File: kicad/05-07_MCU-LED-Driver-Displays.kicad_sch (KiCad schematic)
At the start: 68 parts, among them J4 Conn_02x05_Counter_Clockwise, J5 Conn_01x02_Pin, J6 Conn_01x03_Pin, J7 Conn_01x03_Pin, Q4 AO3400A, Q5 AO3400A, SW1 BOOTSEL, SW2 RESET, SW3 USER_A, SW4 USER_B_PWR, U5 W25Q128JVS, U6 PCF8523T, U7 RP2040, Y1 ABS07AIG-32.768KHZ-7-T, Y2 ABM8-272-T3

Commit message: DR SYS-04-Battery Protect ✅
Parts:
- R19, R20, R21, R22, R23, R24, R25, R26, R27, R28, R29, R30, R31, R32, R33, R34, R35, R36, R37, R38, R39: MPN (none) -> (Generic)
- renumbered JP12 to JP14, JP13 to JP15, JP14 to JP16, JP15 to JP17, JP16 to JP18, JP17 to JP19, JP18 to JP20, JP19 to JP21, TP17 to TP18, TP18 to TP19, TP19 to TP20, TP20 to TP21, TP21 to TP22, TP22 to TP23

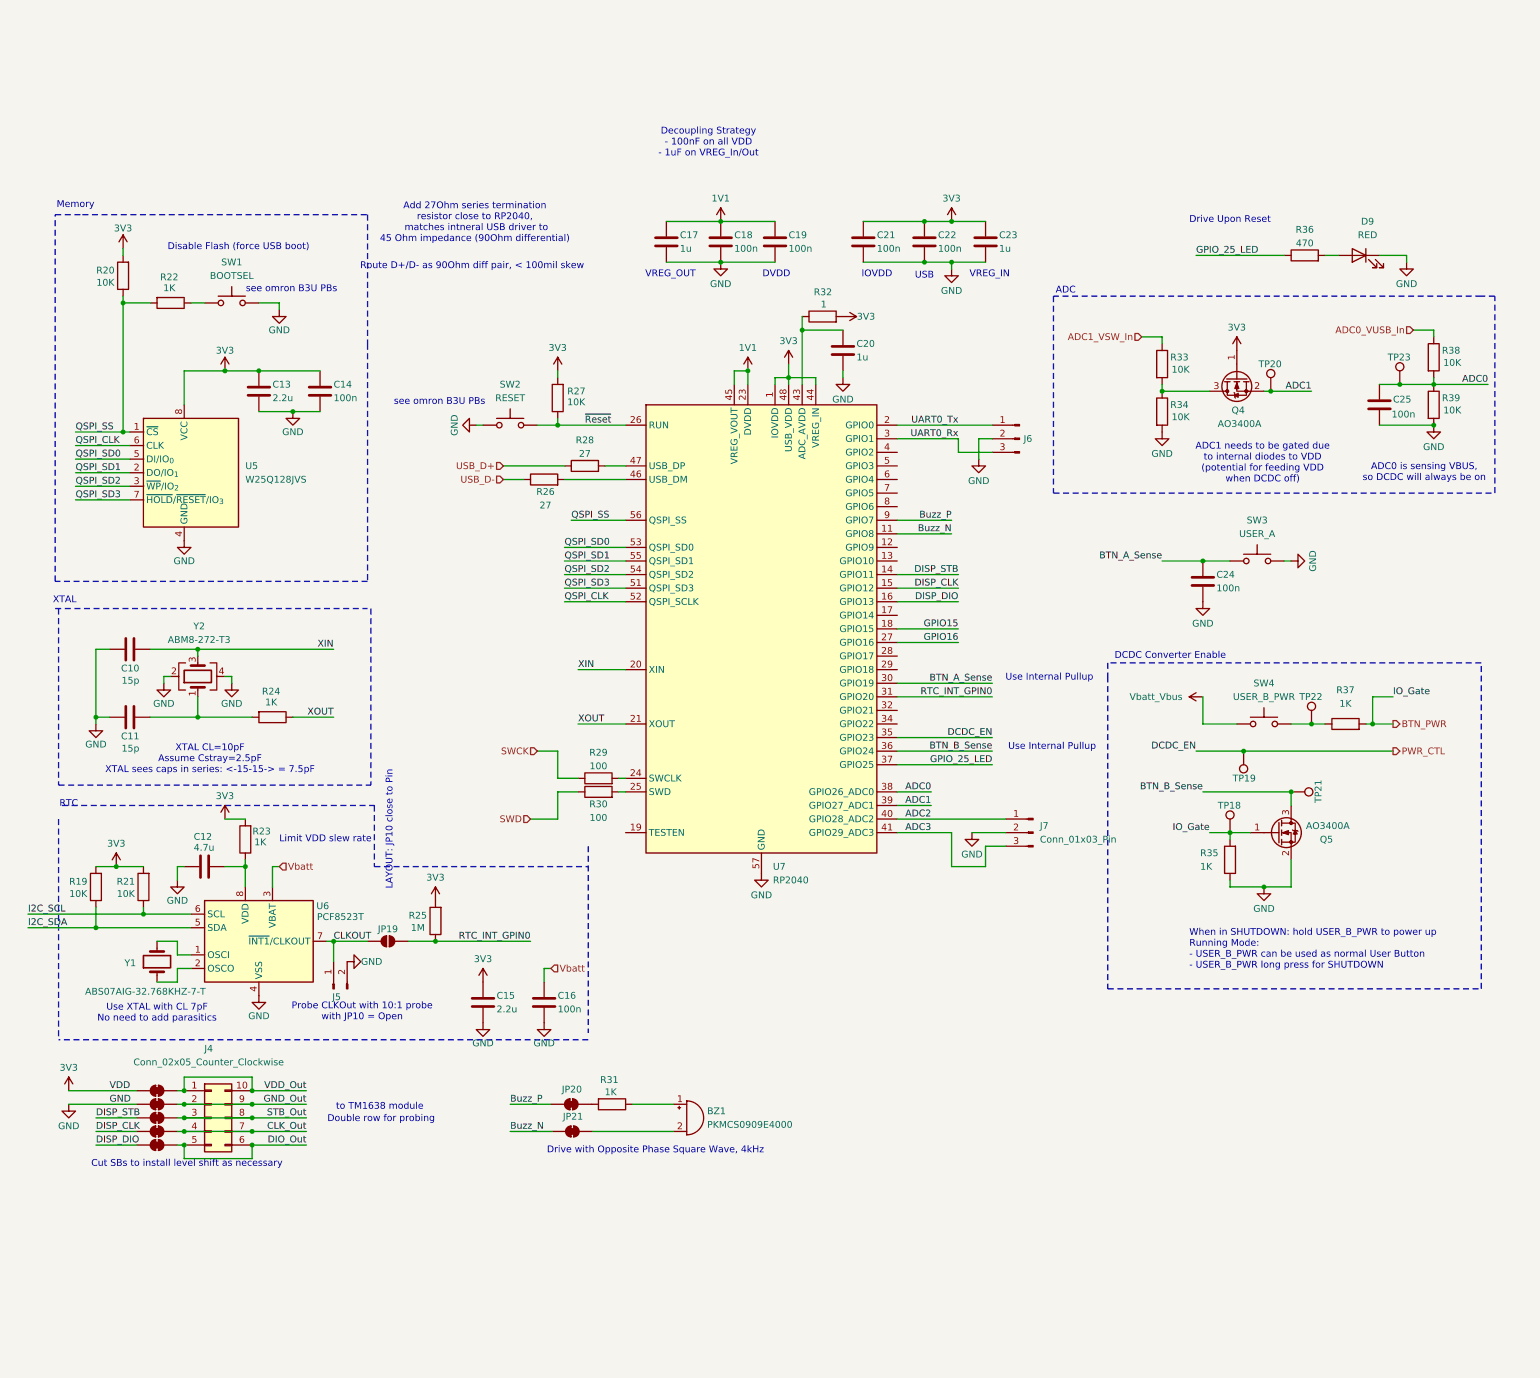
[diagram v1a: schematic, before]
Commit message: DR SYS-05-MCU XTAL
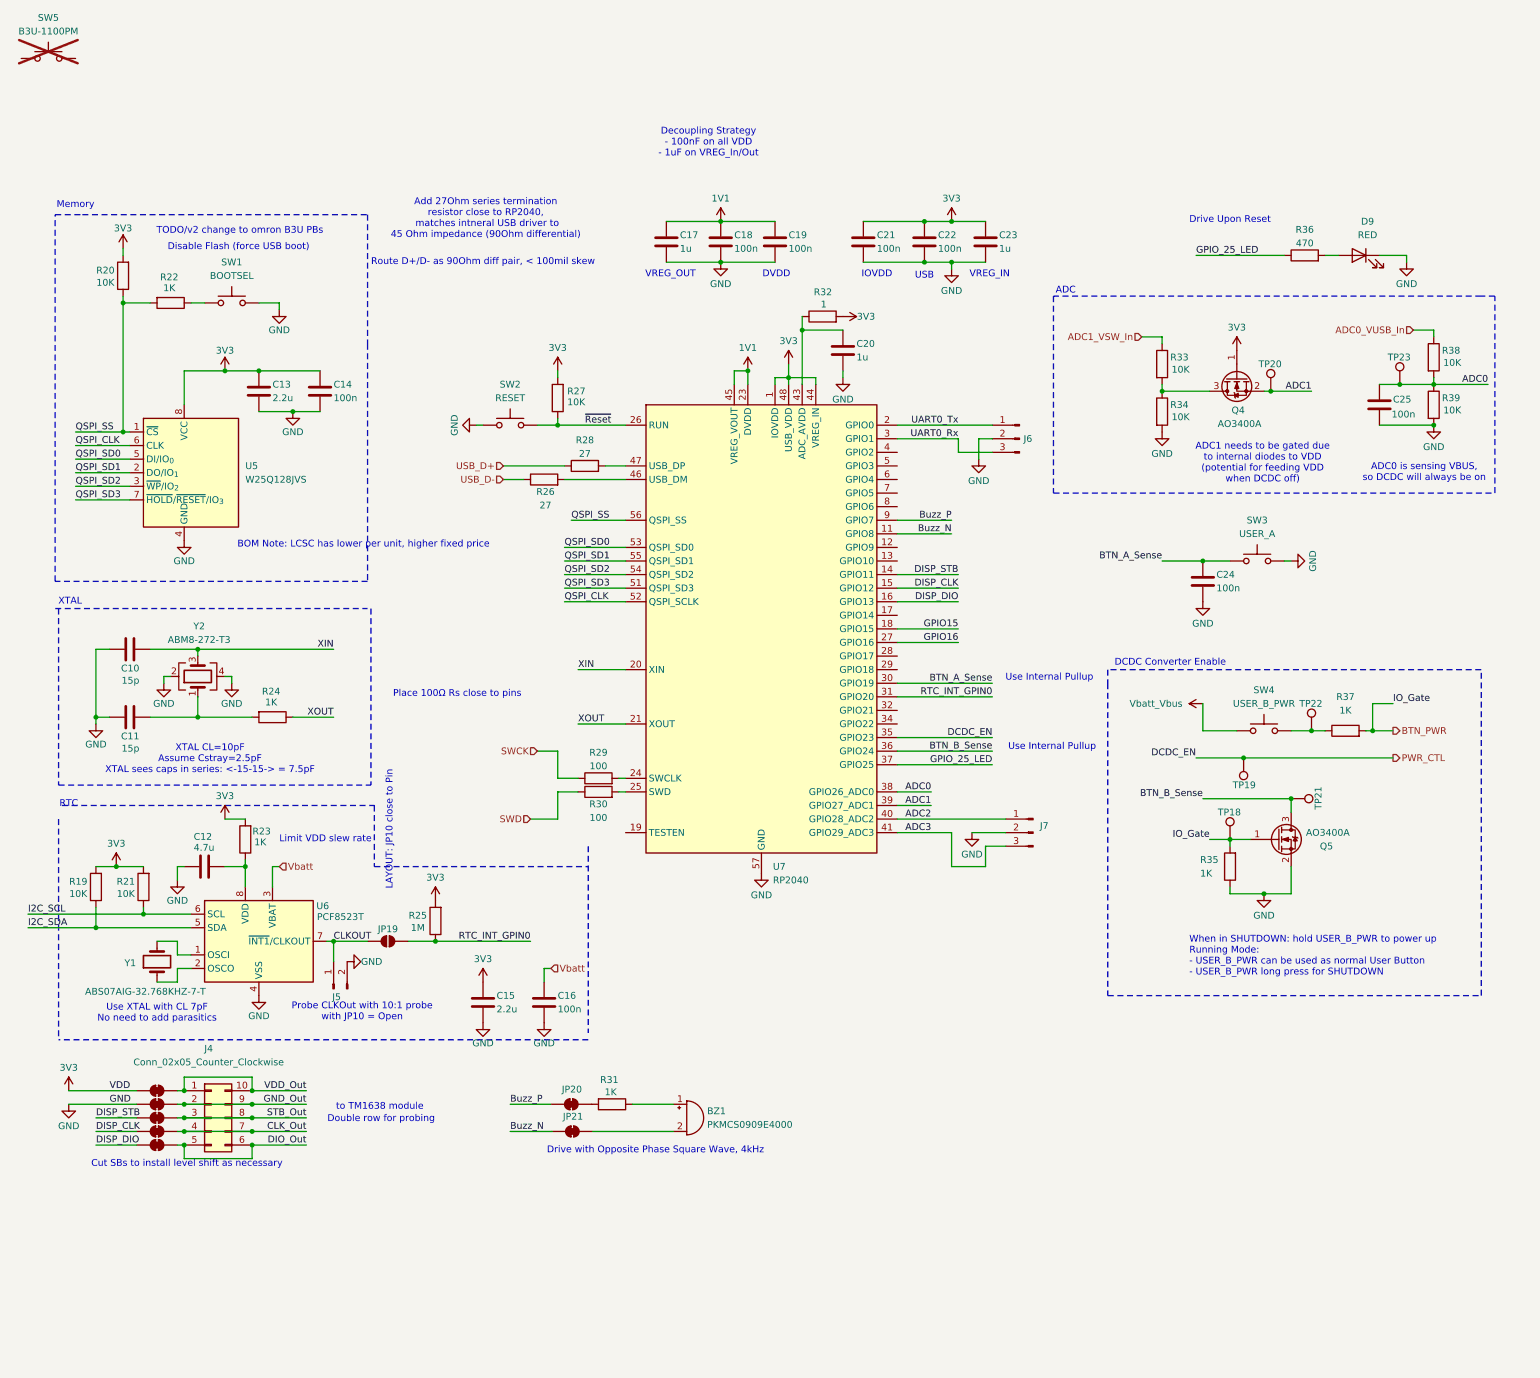
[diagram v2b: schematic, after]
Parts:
- added SW5: B3U-1100PM, Button_Switch_SMD:SW_SPST_B3U-1100P, symbol Switch:SW_Push
- C10, C11: footprint (none) -> Capacitor_SMD:C_0603_1608Metric_Pad1.08x0.95mm_HandSolder; MPN (none) -> (Generic); Manufacturer (none) -> (Generic); Package (none) -> 0603; Subsystem (none) -> 05-MCU-XTAL-FLASH; Supplier 1 (none) -> (Generic)
- C13, C14, C17, C18, C19, C20, C21, C22, C23: footprint (none) -> Capacitor_SMD:C_0805_2012Metric_Pad1.18x1.45mm_HandSolder; MPN (none) -> (Generic); Manufacturer (none) -> (Generic); Package (none) -> 0805; Subsystem (none) -> 05-MCU-XTAL-FLASH; Supplier 1 (none) -> (Generic)
- R20, R22, R24, R27, R29, R30, R32: Manufacturer (none) -> (Generic); Package (none) -> 0805; Subsystem (none) -> 05-MCU-XTAL-FLASH; Supplier 1 (none) -> (Generic)
- SW1, SW2: footprint (none) -> Button_Switch_THT:SW_PUSH_6mm; MPN (none) -> (Generic); Manufacturer (none) -> (Generic); Subsystem (none) -> 05-MCU-XTAL-FLASH; Supplier 1 (none) -> (Generic)
- SW3, SW4: footprint (none) -> Button_Switch_THT:SW_PUSH_6mm; MPN (none) -> (Generic); Manufacturer (none) -> (Generic); Supplier 1 (none) -> (Generic)
- U5: MPN (none) -> W25Q128JVSIQ; Package (none) -> SOIC-8; Subsystem (none) -> 05-MCU-XTAL-FLASH; Supplier 1 LCSC -> Digikey; Supplier 1 SKU C113767 -> (none); Supplier 1 URL https://lcsc.com/product-detail/NOR-FLASH_Winbond-Elec-W25Q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 -> https://www.digikey.jp/en/products/detail/winbond-electroni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; Supplier 2 (none) -> LCSC; Supplier 2 SKU (none) -> C113767; Supplier 2 URL (none) -> https://lcsc.com/product-detail/NOR-FLASH_Winbond-Elec-W25Q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
- U7: Package (none) -> QFN-56-1EP; Subsystem (none) -> 05-MCU-XTAL-FLASH
- Y2: Subsystem (none) -> 05-MCU-XTAL-FLASH
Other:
- note added: "BOM Note: LCSC has lower per unit, higher fixed price"
- note added: "Place 100Ω Rs close to pins"
- note added: "TODO/v2 change to omron B3U PBs"
- note removed: "see omron B3U PBs"
- moved on the sheet: Q5, R35, R37, SW4, TP18, TP19, TP21, TP22

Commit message: DR SYS-06-MCU-IO ✅
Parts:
- added BZ2: Buzzer D=9mm P=5mm, project footprints:Buz-TH_D9.6_P5, symbol Device:Buzzer
- added J9: Conn_01x12_Pin, Connector_PinHeader_2.54mm:PinHeader_1x12_P2.54mm_Vertical, symbol Connector:Conn_01x12_Pin
- added JP22: SolderJumper_2_Open, Jumper:SolderJumper-2_P1.3mm_Open_RoundedPad1.0x1.5mm, symbol Jumper:SolderJumper_2_Open
- added R40: 10K, Resistor_SMD:R_0805_2012Metric_Pad1.20x1.40mm_HandSolder, symbol Device:R
- BZ1: footprint (none) -> project footprints:SPKR_PKMCS0909E4000-R1; Subsystem (none) -> 06-MCU-IO
- C24, C25: footprint (none) -> Capacitor_SMD:C_0805_2012Metric_Pad1.18x1.45mm_HandSolder; MPN (none) -> (Generic); Manufacturer (none) -> (Generic); Package (none) -> 0805; Subsystem (none) -> 06-MCU-IO; Supplier 1 (none) -> (Generic)
- D9: value RED -> RED/USER; MPN (none) -> NCD0805R1; Manufacturer (none) -> Foshan NationStar Optoelectronics; Package (none) -> 0805; Subsystem (none) -> 06-MCU-IO; Supplier 1 (none) -> LCSC; Supplier 1 SKU (none) -> C84256; Supplier 1 URL (none) -> https://lcsc.com/product-detail/Light-Emitting-Diodes-LED_F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
- J6, J7: footprint (none) -> Connector_PinHeader_2.54mm:PinHeader_1x03_P2.54mm_Vertical; MPN (none) -> (Embedded); Subsystem (none) -> 06-MCU-IO
- JP20, JP21: Subsystem (none) -> 06-MCU-IO
- Q4, Q5: MPN (none) -> AO3400A; Manufacturer (none) -> Alpha & Omega Semicon; Package (none) -> SOT-23; Subsystem (none) -> 06-MCU-IO; Supplier 1 (none) -> LCSC; Supplier 1 SKU (none) -> C20917; Supplier 1 URL (none) -> https://jlcpcb.com/partdetail/Alpha_OmegaSemicon-AO3400A/C2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
- R31, R33, R34, R35, R36, R37, R38, R39: Package (none) -> 0805; Subsystem (none) -> 06-MCU-IO
- SW3, SW4: Package (none) -> PB_6x6; Subsystem (none) -> 06-MCU-IO
- TP18: value TestPoint -> IOGate; Subsystem (none) -> 06-MCU-IO
- TP20: value TestPoint -> ADC1; Subsystem (none) -> 06-MCU-IO
- TP21: value TestPoint -> BTN_B; Subsystem (none) -> 06-MCU-IO
- TP22: value TestPoint -> BTN_B_IN; Subsystem (none) -> 06-MCU-IO
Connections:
- net 3V3: now also J9.1 (Pin_1), JP22.1 (A)
- net GND: now also BZ2.2 (-), J9.12 (Pin_12)
- net RTC_INT_GPIN0: now also R40.1
- net AVDD: now reaches C20.1, R32.1, U7.43 (ADC_AVDD)
- net IO9: now reaches U7.12 (GPIO9)
- net IO9: now also J9.6 (Pin_6)
- net IO10: now reaches U7.13 (GPIO10)
- net IO14: now reaches U7.17 (GPIO14)
- net IO14: now also J9.7 (Pin_7)
- net IO17: now reaches U7.28 (GPIO17)
- net IO17: now also J9.8 (Pin_8)
- net IO18: now reaches U7.29 (GPIO18)
- net IO18: now also J9.9 (Pin_9)
- net IO21: now reaches U7.32 (GPIO21)
- net IO21: now also J9.10 (Pin_10)
- net IO22: now reaches U7.34 (GPIO22)
- net IO22: now also J9.11 (Pin_11)
- net IO2: now reaches U7.4 (GPIO2)
- net IO2: now also J9.2 (Pin_2)
- net IO3: now reaches U7.5 (GPIO3)
- net IO3: now also J9.3 (Pin_3)
- net IO4: now reaches U7.6 (GPIO4)
- net IO4: now also J9.4 (Pin_4)
- net IO5: now reaches U7.7 (GPIO5)
- net IO5: now also J9.5 (Pin_5)
- net BZ1: now reaches U7.8 (GPIO6)
- net BZ1: now also BZ2.1 (+)
- net Buzz_N renamed BZ2_N
- net Buzz_P renamed BZ2_P
- net GPIO_25_LED renamed IO25_LED
- new net: JP22.2 (B), R40.2
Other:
- note added: "*"
- note added: "*Use Internal Pullup"
- note added: "Decrease Rpu to use CLKOUT"
- note removed: "Use Internal Pullup"
- moved on the sheet: BZ1, JP20, JP21, R25, R31
